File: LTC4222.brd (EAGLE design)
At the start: 55.9 x 59.4 mm, 45 parts, among them IC1 67997-100HLF, IC2 LTC4222, J1 PMV15ENEAR, J2 PMV15ENEAR, P1 S1751-46R, P11 S1751-46R, P12 S1751-46R, P13 S1751-46R, P14 S1751-46R, P15 S1751-46R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

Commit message: PCB schematic V1.2
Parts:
- added JP4: (no value), pinhead:1X08
- moved P18 14.6 mm to (4.06, 25.5)
- moved C4 13.0 mm to (20.3, 23.9)
- moved C3 12.8 mm to (21.0, 33.5)
- moved P8 8.42 mm to (37.8, 37.2), turned to 90 degrees
- moved JP2 8.33 mm to (17.9, 47.4)
- moved R7 8.24 mm to (33.3, 34.8), turned to 0 degrees
- moved C1 7.98 mm to (20.4, 41.7)
- moved R4 7.93 mm to (21.1, 37.7)
- moved R2 7.78 mm to (23.4, 45.0)
- moved R6 7.64 mm to (35.8, 39.5)
- moved R8 7.09 mm to (40.0, 39.9)
- moved R3 6.65 mm to (23.4, 39.9)
- moved P3 6.38 mm to (24.0, 35.6), turned to 180 degrees
- moved P12 5.97 mm to (35.4, 20.8)
- moved P4 5.59 mm to (30.0, 51.2), turned to 180 degrees
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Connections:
- new net N$3: IC2.24, JP4.1
- new net N$4: IC2.20, JP4.5
- new net N$5: IC2.19, JP4.6
- new net N$9: IC2.17, JP4.8
- net ADIN1: now also JP4.2
- net ADIN2: now also JP4.7
- net ALERT: now also JP4.4
- net ON: now also JP4.3
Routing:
- net N$16: track 19.0 -> 5.55 mm
- net N$15: track 18.3 -> 5.58 mm
- net N$19: track 23.7 -> 12.4 mm
- net N$12: track 45.5 -> 35.1 mm
- net N$14: track 28.4 -> 18.3 mm
- net N$8: track 33.1 -> 23.9 mm
- net N$2: track 41.7 -> 33.5 mm
- net N$29: track 25.0 -> 18.7 mm
- net N$6: track 26.2 -> 20.8 mm
- net N$7: track 22.4 -> 17.1 mm
- net N$10: track 13.3 -> 9.14 mm
- net GND: track 8.98 -> 5.50 mm
- net N$11: track 21.8 -> 18.7 mm
- net N$31: track 15.6 -> 12.9 mm
- net N$30: track 14.6 -> 12.0 mm
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
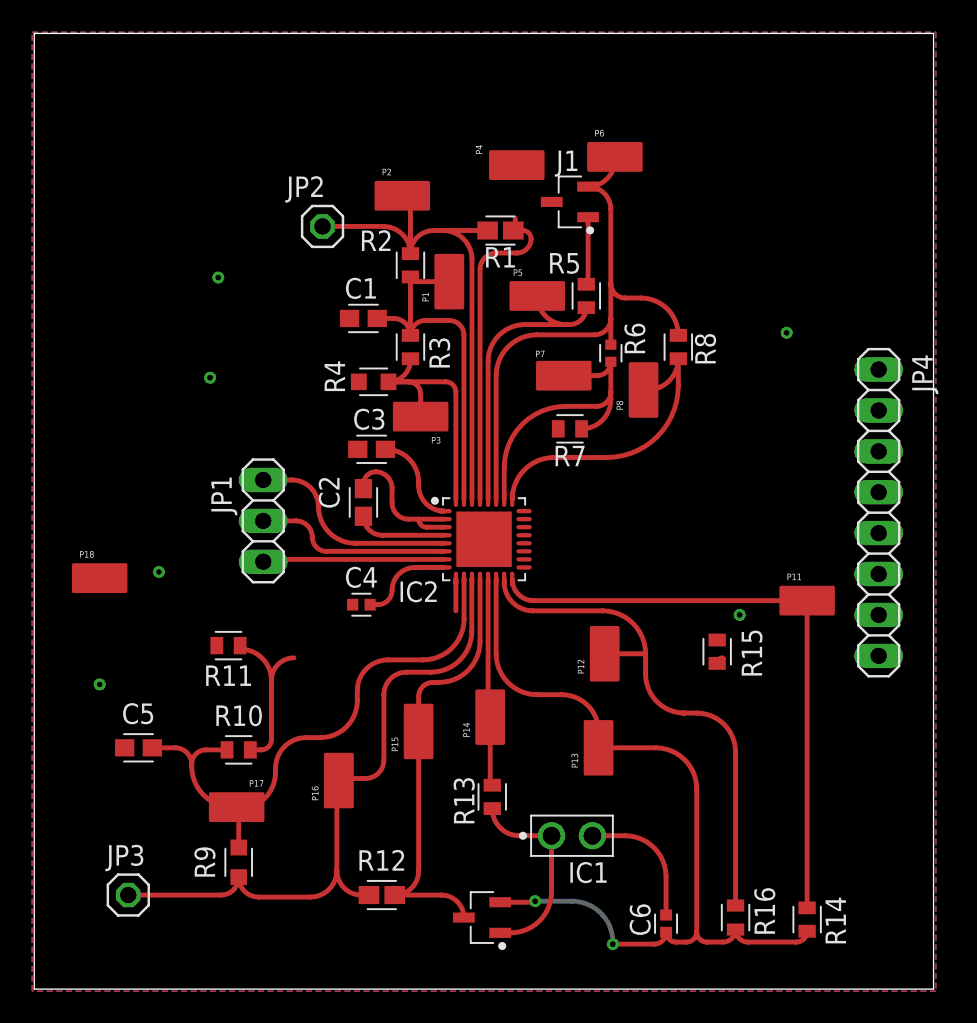
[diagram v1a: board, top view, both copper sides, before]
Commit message: LTC4222 v1.9; requires ground vias everywhere; idk how to un ratsnets the ground
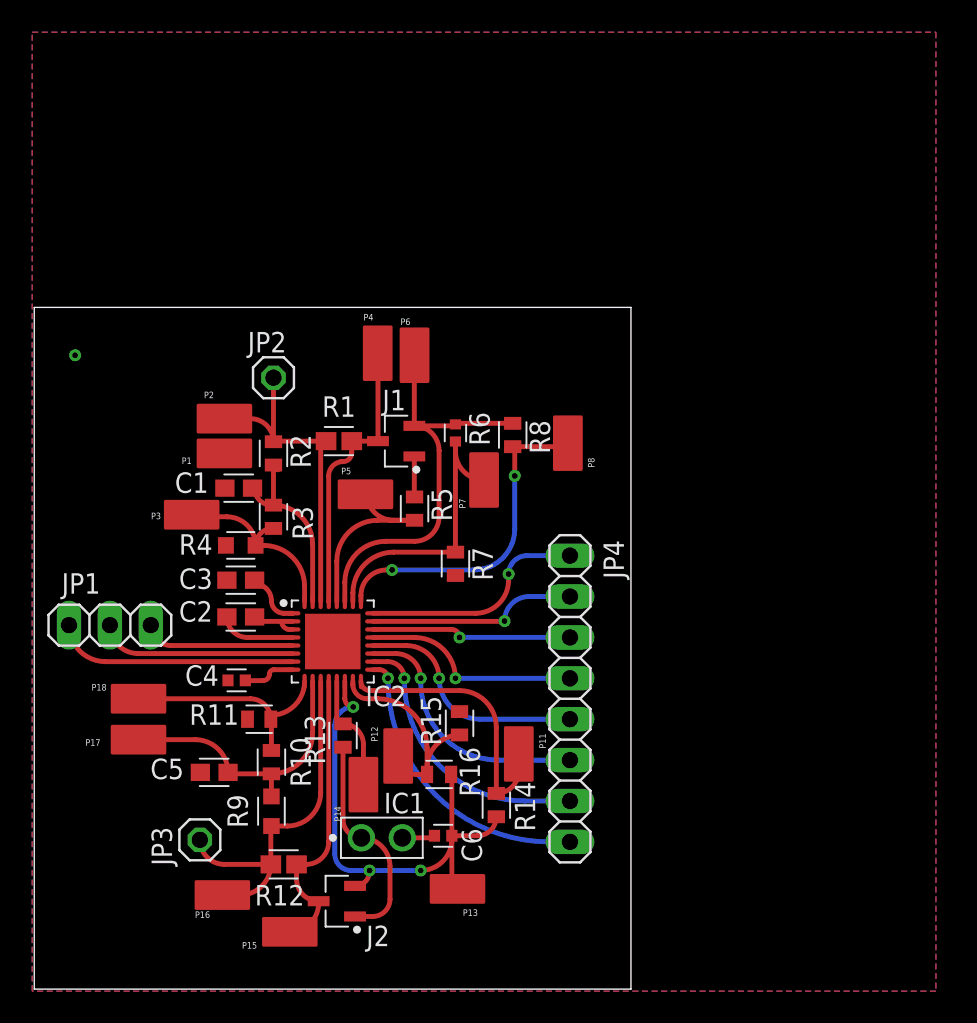
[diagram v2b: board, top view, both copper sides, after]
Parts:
- moved JP4 22.4 mm to (33.3, 18.0)
- moved R14 20.6 mm to (28.7, 11.4)
- moved R16 20.4 mm to (25.1, 13.3), turned to 180 degrees
- moved P11 20.3 mm to (30.1, 14.6), turned to 270 degrees
- moved J1 18.4 mm to (22.5, 34.0)
- moved P2 17.7 mm to (11.8, 35.4)
- moved P1 17.6 mm to (11.8, 33.3), turned to 180 degrees
- moved P6 17.5 mm to (23.6, 39.4), turned to 90 degrees
- moved R5 17.0 mm to (23.6, 29.8)
- moved R15 16.6 mm to (26.4, 16.5)
- moved R1 16.5 mm to (18.9, 34.0)
- moved P5 16.3 mm to (20.6, 30.7)
- moved P3 15.5 mm to (9.78, 29.5)
- moved C6 14.9 mm to (25.4, 9.53), turned to 0 degrees
- moved P15 14.8 mm to (15.9, 3.56), turned to 180 degrees
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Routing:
- net N$26: track 38.0 -> 16.7 mm
- net N$23: track 52.5 -> 32.1 mm, vias 2 -> 3
- net N$21: track 40.9 -> 21.6 mm
- net N$25: track 32.4 -> 14.1 mm
- net N$27: track 35.2 -> 17.3 mm
- net N$9: track 0.00 -> 16.8 mm, vias 0 -> 1
- net ADIN2: track 0.00 -> 15.9 mm, vias 0 -> 1
- net N$5: track 0.00 -> 15.1 mm, vias 0 -> 1
- net N$4: track 0.00 -> 14.1 mm, vias 0 -> 1
- net N$3: track 0.00 -> 14.0 mm, vias 0 -> 1
- net ALERT: track 0.00 -> 13.3 mm, vias 0 -> 1
- net ADIN1: track 0.00 -> 12.9 mm, vias 0 -> 1
- net ON: track 0.00 -> 12.5 mm, vias 0 -> 1
- net N$8: track 23.9 -> 11.9 mm
- net N$2: track 33.5 -> 21.9 mm
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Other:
- board size 55.9 x 59.4 mm -> 37.1 x 42.3 mm

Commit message: LTC4222 V2
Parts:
- moved P15 4.28 mm to (11.7, 4.45)
- moved JP3 2.10 mm to (12.2, 10.2)
- moved P16 0.89 mm to (11.7, 6.73)
- moved P17 0.38 mm to (6.48, 15.9)
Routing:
- net N$20: track 18.0 -> 21.8 mm
- net N$21: track 21.6 -> 19.7 mm
- net GND: vias 1 -> 47
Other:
- board size 37.1 x 42.3 mm -> 36.2 x 42.3 mm
